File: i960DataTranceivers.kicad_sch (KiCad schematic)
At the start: 6 parts

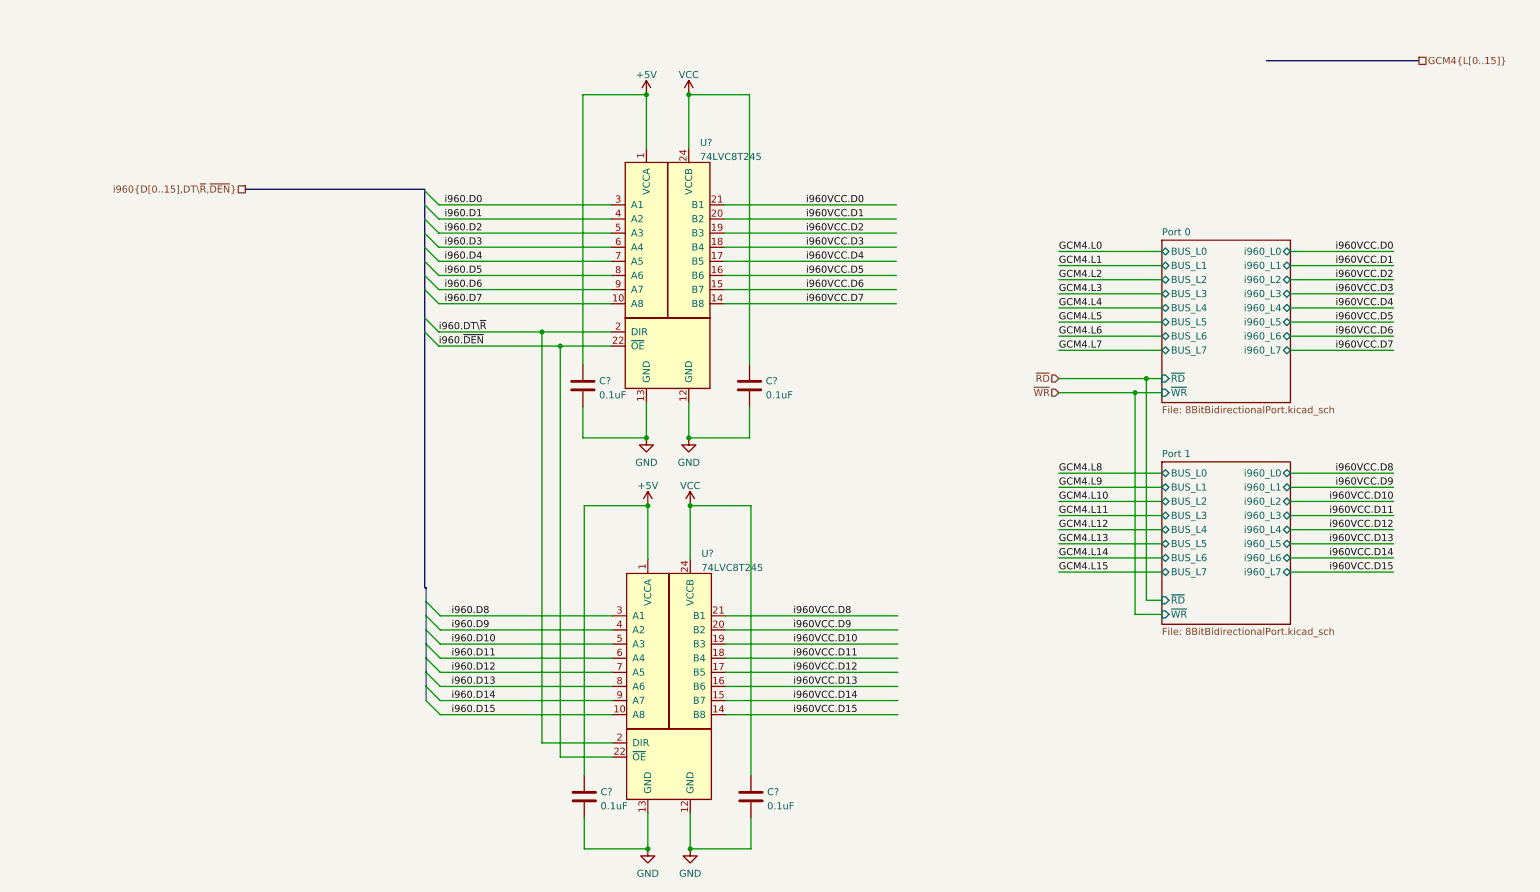
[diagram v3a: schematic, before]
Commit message: Instead of using a double buffer design, just connect the bus selector and DEN lines together with an or gate.
That way we keep the transceivers off of the bus.
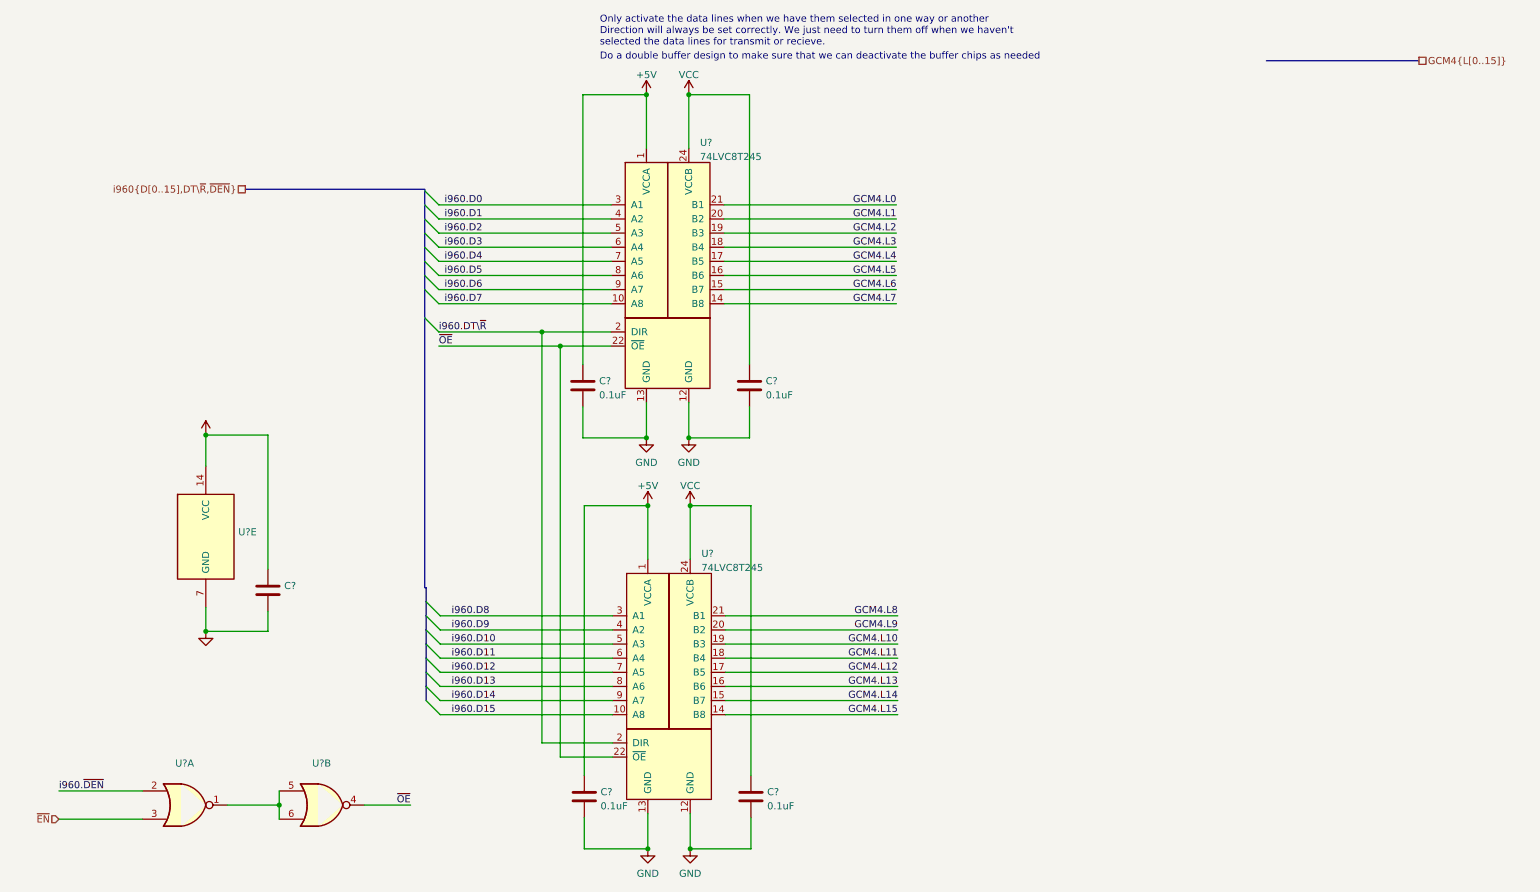
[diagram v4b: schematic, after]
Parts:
- added C?: (no value), symbol Device:C
- added U? (x3): (no value), symbol 74xx:74HC02
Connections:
- net i960VCC.D0 is gone; now on net GCM4.L0: U?.21 (B1)
- net i960VCC.D1 is gone; now on net GCM4.L1: U?.20 (B2)
- net i960VCC.D10 is gone; now on net GCM4.L10: U?.19 (B3)
- net i960VCC.D11 is gone; now on net GCM4.L11: U?.18 (B4)
- net i960VCC.D12 is gone; now on net GCM4.L12: U?.17 (B5)
- net i960VCC.D13 is gone; now on net GCM4.L13: U?.16 (B6)
- net i960VCC.D14 is gone; now on net GCM4.L14: U?.15 (B7)
- net i960VCC.D15 is gone; now on net GCM4.L15: U?.14 (B8)
- net i960VCC.D2 is gone; now on net GCM4.L2: U?.19 (B3)
- net i960VCC.D3 is gone; now on net GCM4.L3: U?.18 (B4)
- net i960VCC.D4 is gone; now on net GCM4.L4: U?.17 (B5)
- net i960VCC.D5 is gone; now on net GCM4.L5: U?.16 (B6)
- net i960VCC.D6 is gone; now on net GCM4.L6: U?.15 (B7)
- net i960VCC.D7 is gone; now on net GCM4.L7: U?.14 (B8)
- net i960VCC.D8 is gone; now on net GCM4.L8: U?.21 (B1)
- net i960VCC.D9 is gone; now on net GCM4.L9: U?.20 (B2)
- net +5V: now also C?.1, U?.14 (VCC)
- net GND: now also C?.2, U?.7 (GND)
- net i960.~{DEN}: now also U?.2; no longer U?.22 (~{OE}), U?.22 (~{OE})
- new net: U?.1, U?.5, U?.6
- new net ~{EN}: U?.3
- new net ~{OE}: U?.22 (~{OE}), U?.22 (~{OE}), U?.4
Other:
- removed sheet Port 0
- removed sheet Port 1
- note added: "Do a double buffer design to make sure that we can deactivate the buffer chips as needed"
- note added: "Only activate the data lines when we have them selected in one way or another Direction will always be set correctly. We just need to turn them off when we haven't selected the data lines for transmit or recieve."

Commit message: Initial layout complete
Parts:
- gave numbers to parts that had none: 8
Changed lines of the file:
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@@
   (symbol (lib_id "NewICs:74LVC8T245") (at 126.746 66.548 0) (unit 1)
     (in_bom yes) (on_board yes) (fields_autoplaced)
-    (property "Reference" "U?" (id 0) (at 132.5754 33.7652 0)
+    (property "Reference" "U7" (id 0) (at 132.5754 33.7652 0)
       (effects (font (size 1.27 1.27)) (justify left))
     )
@@
   (symbol (lib_id "power:GND") (at 130.556 86.868 0) (unit 1)
     (in_bom yes) (on_board yes) (fields_autoplaced)
-    (property "Reference" "#PWR?" (id 0) (at 130.556 93.218 0)
+    (property "Reference" "#PWR0123" (id 0) (at 130.556 93.218 0)
       (effects (font (size 1.27 1.27)) hide)
     )
@@
   (symbol (lib_id "74xx:74HC02") (at 64.516 152.908 0) (unit 2)
     (in_bom yes) (on_board yes) (fields_autoplaced)
-    (property "Reference" "U?" (id 0) (at 64.516 145.3982 0))
+    (property "Reference" "U6" (id 0) (at 64.516 145.3982 0))
     (property "Value" "" (id 1) (at 64.516 147.9351 0))
     (property "Footprint" "" (id 2) (at 64.516 152.908 0)
@@
   (symbol (lib_id "Device:C") (at 141.732 151.384 0) (unit 1)
     (in_bom yes) (on_board yes) (fields_autoplaced)
-    (property "Reference" "C?" (id 0) (at 144.653 150.5493 0)
+    (property "Reference" "C10" (id 0) (at 144.653 150.5493 0)
       (effects (font (size 1.27 1.27)) (justify left))
     )
@@
   (symbol (lib_id "power:GND") (at 123.19 160.782 0) (unit 1)
     (in_bom yes) (on_board yes) (fields_autoplaced)
-    (property "Reference" "#PWR?" (id 0) (at 123.19 167.132 0)
+    (property "Reference" "#PWR0119" (id 0) (at 123.19 167.132 0)
       (effects (font (size 1.27 1.27)) hide)
     )
@@
   (symbol (lib_id "power:GND") (at 43.688 121.666 0) (unit 1)
     (in_bom yes) (on_board yes) (fields_autoplaced)
-    (property "Reference" "#PWR?" (id 0) (at 43.688 128.016 0)
+    (property "Reference" "#PWR0125" (id 0) (at 43.688 128.016 0)
       (effects (font (size 1.27 1.27)) hide)
     )
@@
   (symbol (lib_id "power:+5V") (at 122.936 25.146 0) (unit 1)
     (in_bom yes) (on_board yes) (fields_autoplaced)
-    (property "Reference" "#PWR?" (id 0) (at 122.936 28.956 0)
+    (property "Reference" "#PWR0117" (id 0) (at 122.936 28.956 0)
       (effects (font (size 1.27 1.27)) hide)
     )
@@
   (symbol (lib_id "power:GND") (at 122.936 86.868 0) (unit 1)
     (in_bom yes) (on_board yes) (fields_autoplaced)
-    (property "Reference" "#PWR?" (id 0) (at 122.936 93.218 0)
+    (property "Reference" "#PWR0122" (id 0) (at 122.936 93.218 0)
       (effects (font (size 1.27 1.27)) hide)
     )
@@
   (symbol (lib_id "Device:C") (at 111.76 151.384 0) (unit 1)
     (in_bom yes) (on_board yes) (fields_autoplaced)
-    (property "Reference" "C?" (id 0) (at 114.681 150.5493 0)
+    (property "Reference" "C8" (id 0) (at 114.681 150.5493 0)
       (effects (font (size 1.27 1.27)) (justify left))
     )
@@
   (symbol (lib_id "power:GND") (at 130.81 160.782 0) (unit 1)
     (in_bom yes) (on_board yes) (fields_autoplaced)
-    (property "Reference" "#PWR?" (id 0) (at 130.81 167.132 0)
+    (property "Reference" "#PWR0120" (id 0) (at 130.81 167.132 0)
       (effects (font (size 1.27 1.27)) hide)
     )
@@
   (symbol (lib_id "power:VCC") (at 130.81 99.06 0) (unit 1)
     (in_bom yes) (on_board yes) (fields_autoplaced)
-    (property "Reference" "#PWR?" (id 0) (at 130.81 102.87 0)
+    (property "Reference" "#PWR0124" (id 0) (at 130.81 102.87 0)
       (effects (font (size 1.27 1.27)) hide)
     )
@@
   (symbol (lib_id "power:+5V") (at 123.19 99.06 0) (unit 1)
     (in_bom yes) (on_board yes) (fields_autoplaced)
-    (property "Reference" "#PWR?" (id 0) (at 123.19 102.87 0)
+    (property "Reference" "#PWR0121" (id 0) (at 123.19 102.87 0)
       (effects (font (size 1.27 1.27)) hide)
     )
@@
   (symbol (lib_id "Device:C") (at 141.478 77.47 0) (unit 1)
     (in_bom yes) (on_board yes) (fields_autoplaced)
-    (property "Reference" "C?" (id 0) (at 144.399 76.6353 0)
+    (property "Reference" "C9" (id 0) (at 144.399 76.6353 0)
       (effects (font (size 1.27 1.27)) (justify left))
     )
@@
   (symbol (lib_id "NewICs:74LVC8T245") (at 127 140.462 0) (unit 1)
     (in_bom yes) (on_board yes) (fields_autoplaced)
-    (property "Reference" "U?" (id 0) (at 132.8294 107.6792 0)
+    (property "Reference" "U8" (id 0) (at 132.8294 107.6792 0)
       (effects (font (size 1.27 1.27)) (justify left))
     )
@@
   (symbol (lib_id "74xx:74HC02") (at 39.878 152.908 0) (unit 1)
     (in_bom yes) (on_board yes) (fields_autoplaced)
-    (property "Reference" "U?" (id 0) (at 39.878 145.3982 0))
+    (property "Reference" "U6" (id 0) (at 39.878 145.3982 0))
     (property "Value" "" (id 1) (at 39.878 147.9351 0))
     (property "Footprint" "" (id 2) (at 39.878 152.908 0)
@@
   (symbol (lib_id "Device:C") (at 111.506 77.47 0) (unit 1)
     (in_bom yes) (on_board yes) (fields_autoplaced)
-    (property "Reference" "C?" (id 0) (at 114.427 76.6353 0)
+    (property "Reference" "C7" (id 0) (at 114.427 76.6353 0)
       (effects (font (size 1.27 1.27)) (justify left))
     )
@@
   (symbol (lib_id "74xx:74HC02") (at 43.688 104.648 0) (unit 5)
     (in_bom yes) (on_board yes) (fields_autoplaced)
-    (property "Reference" "U?" (id 0) (at 49.53 103.8133 0)
+    (property "Reference" "U6" (id 0) (at 49.53 103.8133 0)
       (effects (font (size 1.27 1.27)) (justify left))
     )
@@
   (symbol (lib_id "power:+5V") (at 43.688 86.36 0) (unit 1)
     (in_bom yes) (on_board yes) (fields_autoplaced)
-    (property "Reference" "#PWR?" (id 0) (at 43.688 90.17 0)
+    (property "Reference" "#PWR0126" (id 0) (at 43.688 90.17 0)
       (effects (font (size 1.27 1.27)) hide)
     )
@@
   (symbol (lib_id "power:VCC") (at 130.556 25.146 0) (unit 1)
     (in_bom yes) (on_board yes) (fields_autoplaced)
-    (property "Reference" "#PWR?" (id 0) (at 130.556 28.956 0)
+    (property "Reference" "#PWR0118" (id 0) (at 130.556 28.956 0)
       (effects (font (size 1.27 1.27)) hide)
     )
@@
   (symbol (lib_id "Device:C") (at 54.864 114.3 0) (unit 1)
     (in_bom yes) (on_board yes) (fields_autoplaced)
-    (property "Reference" "C?" (id 0) (at 57.785 113.4653 0)
-      (effects (font (size 1.27 1.27)) (justify left))
-    )
+    (property "Reference" "C6" (id 0) (at 57.785 113.4653 0)
+      (effects (font (size 1.27 1.27)) (justify left))
+    )

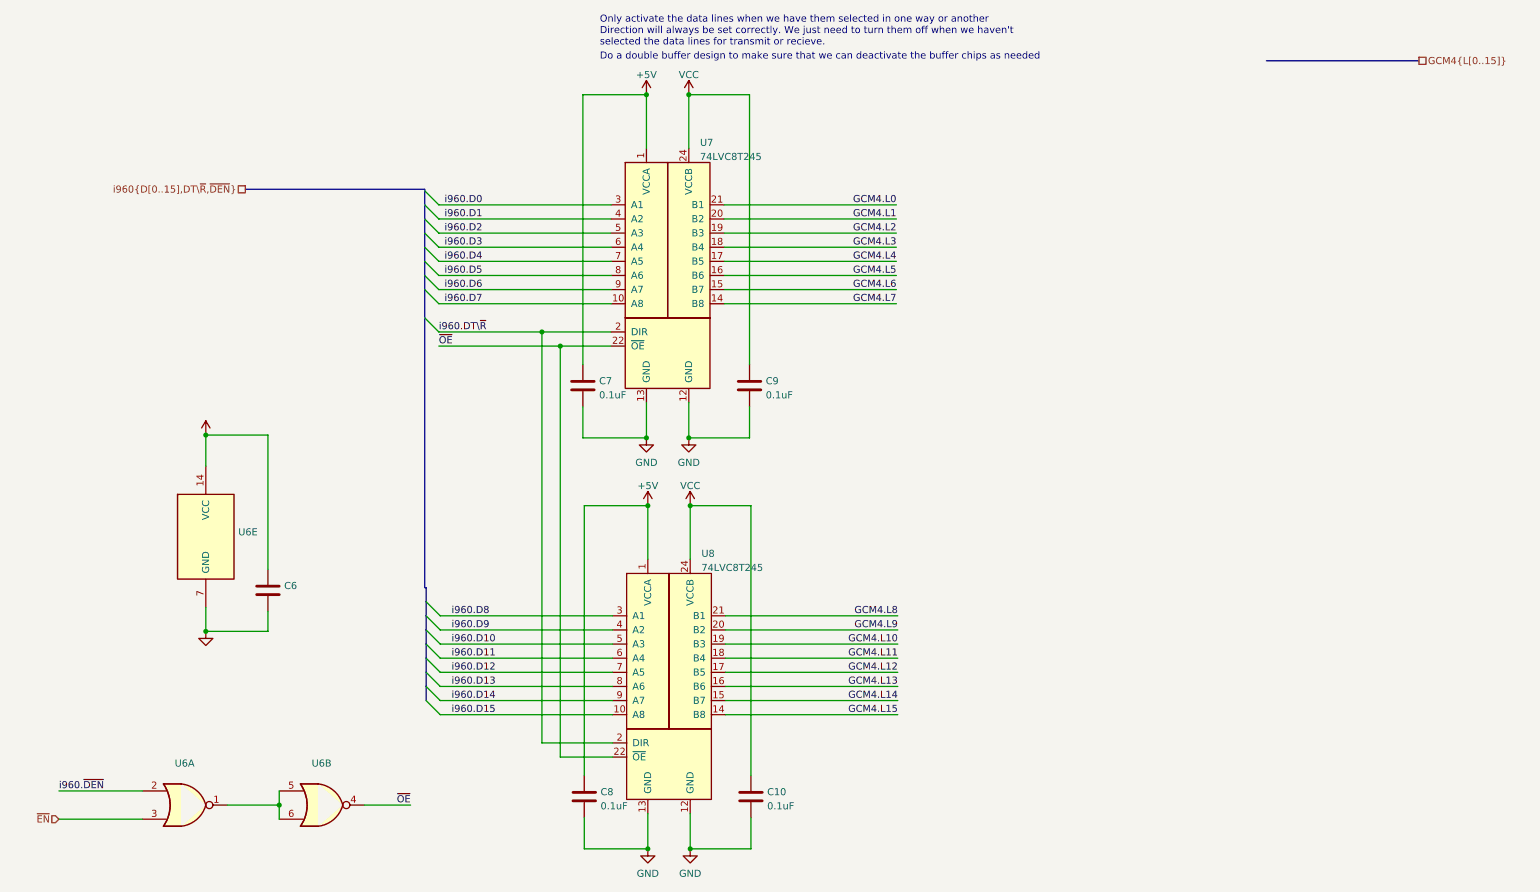
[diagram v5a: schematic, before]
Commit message: use the output enable lines on the latches and buffers to do direct logic level conversion
Save some chips in the process.
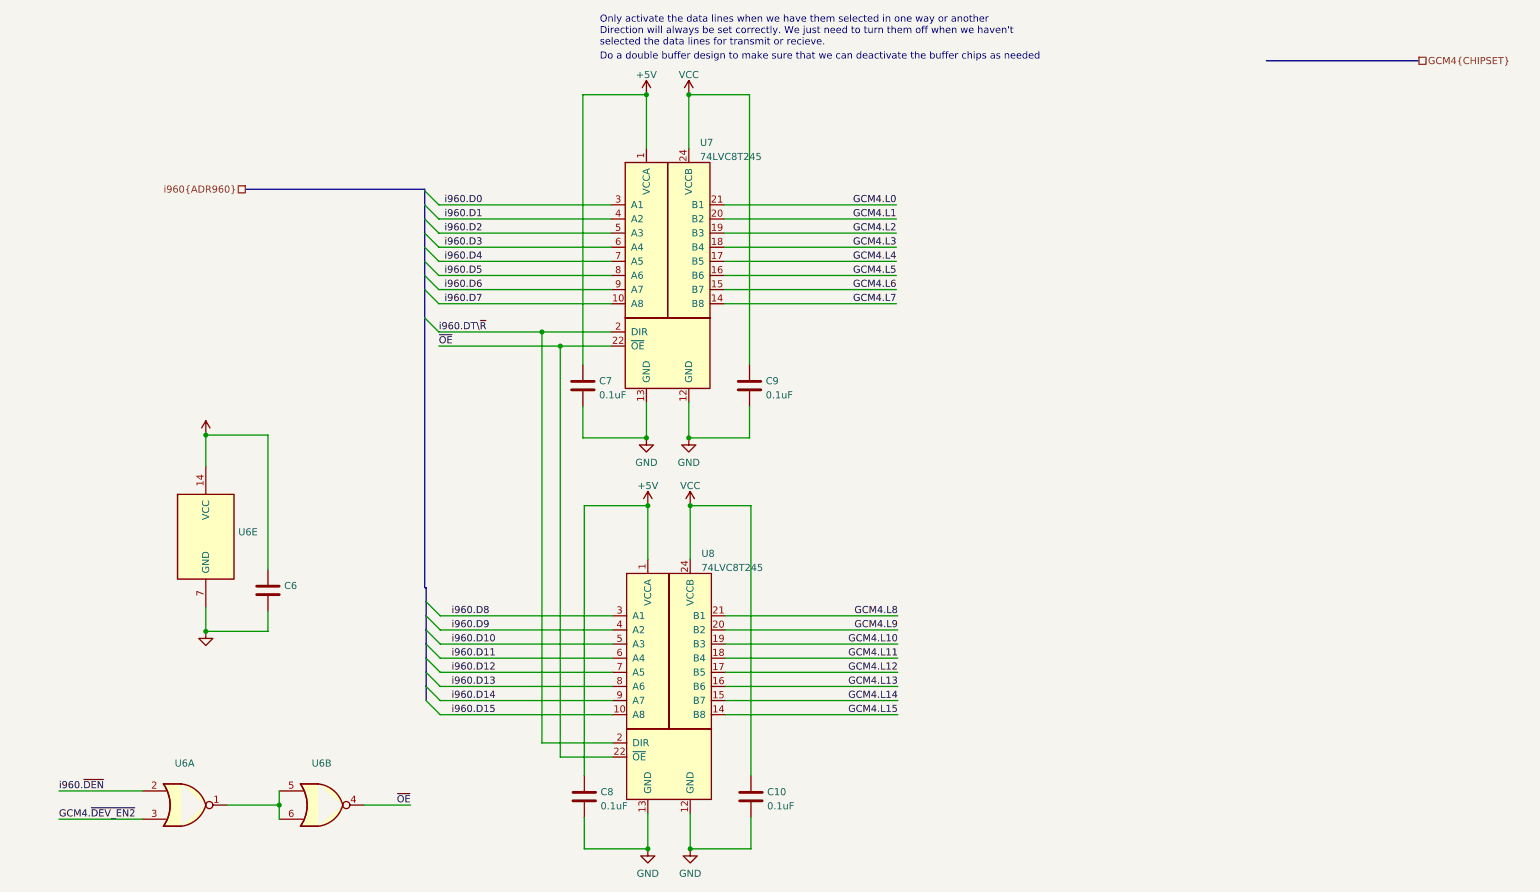
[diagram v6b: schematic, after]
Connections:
- net ~{EN} renamed GCM4.~{DEV_EN2}
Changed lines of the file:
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@@
     (effects (font (size 1.27 1.27)) (justify right bottom))
+  )
+  (label "GCM4.~{DEV_EN2}" (at 17.272 155.448 0)
+    (effects (font (size 1.27 1.27)) (justify left bottom))
   )
   (label "GCM4.L2" (at 167.894 50.038 180)
@@
     (effects (font (size 1.27 1.27)) (justify left bottom))
   )
-  (hierarchical_label "~{EN}" (shape input) (at 17.272 155.448 180)
+  (hierarchical_label "GCM4{CHIPSET}" (shape passive) (at 261.874 19.05 0)
+    (effects (font (size 1.27 1.27)) (justify left))
+  )
+  (hierarchical_label "i960{ADR960}" (shape passive) (at 50.8 42.164 180)
     (effects (font (size 1.27 1.27)) (justify right))
   )
-  (hierarchical_label "GCM4{L[0..15]}" (shape passive) (at 261.874 19.05 0)
-    (effects (font (size 1.27 1.27)) (justify left))
-  )
-  (hierarchical_label "i960{D[0..15],DT\\~{R},~{DEN}}" (shape passive) (at 50.8 42.164 180)
-    (effects (font (size 1.27 1.27)) (justify right))
-  )

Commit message: Do a bulk update and fix all values
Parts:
- C10, C7, C8, C9: value 0.1uF -> (none)
- U7, U8: value 74LVC8T245 -> (none); footprint Package_SO:SOIC-24W_7.5x15.4mm_P1.27mm -> (none)
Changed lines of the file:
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@@
       (effects (font (size 1.27 1.27)) (justify left))
     )
-    (property "Value" "74LVC8T245" (id 1) (at 132.5754 36.3021 0)
-      (effects (font (size 1.27 1.27)) (justify left))
-    )
-    (property "Footprint" "Package_SO:SOIC-24W_7.5x15.4mm_P1.27mm" (id 2) (at 126.746 66.548 0)
+    (property "Value" "" (id 1) (at 132.5754 36.3021 0)
+      (effects (font (size 1.27 1.27)) (justify left))
+    )
+    (property "Footprint" "" (id 2) (at 126.746 66.548 0)
       (effects (font (size 1.27 1.27)) hide)
     )
@@
       (effects (font (size 1.27 1.27)) (justify left))
     )
-    (property "Value" "0.1uF" (id 1) (at 144.653 153.0862 0)
+    (property "Value" "" (id 1) (at 144.653 153.0862 0)
       (effects (font (size 1.27 1.27)) (justify left))
     )
@@
       (effects (font (size 1.27 1.27)) (justify left))
     )
-    (property "Value" "0.1uF" (id 1) (at 114.681 153.0862 0)
+    (property "Value" "" (id 1) (at 114.681 153.0862 0)
       (effects (font (size 1.27 1.27)) (justify left))
     )
@@
       (effects (font (size 1.27 1.27)) (justify left))
     )
-    (property "Value" "0.1uF" (id 1) (at 144.399 79.1722 0)
+    (property "Value" "" (id 1) (at 144.399 79.1722 0)
       (effects (font (size 1.27 1.27)) (justify left))
     )
@@
       (effects (font (size 1.27 1.27)) (justify left))
     )
-    (property "Value" "74LVC8T245" (id 1) (at 132.8294 110.2161 0)
-      (effects (font (size 1.27 1.27)) (justify left))
-    )
-    (property "Footprint" "Package_SO:SOIC-24W_7.5x15.4mm_P1.27mm" (id 2) (at 127 140.462 0)
+    (property "Value" "" (id 1) (at 132.8294 110.2161 0)
+      (effects (font (size 1.27 1.27)) (justify left))
+    )
+    (property "Footprint" "" (id 2) (at 127 140.462 0)
       (effects (font (size 1.27 1.27)) hide)
     )
@@
       (effects (font (size 1.27 1.27)) (justify left))
     )
-    (property "Value" "0.1uF" (id 1) (at 114.427 79.1722 0)
-      (effects (font (size 1.27 1.27)) (justify left))
-    )
+    (property "Value" "" (id 1) (at 114.427 79.1722 0)
+      (effects (font (size 1.27 1.27)) (justify left))
+    )
